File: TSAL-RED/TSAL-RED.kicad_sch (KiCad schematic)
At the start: 49 parts, among them J1 Conn_01x02, J2 Conn_01x02, J3 Conn_02x01, J4 Conn_02x01, K1 G5V-2, Q1 2N7002, Q2 AO3401A, U1 LM358, U2 4N35, U3 NE555D

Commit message: CREATE TSAL PCBs
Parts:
- added J5: Conn_02x01, Connector_Molex:Molex_Micro-Fit_3.0_43045-0212_2x01_P3.00mm_Vertical, symbol Connector_Generic:Conn_02x01
- J1, J2: footprint Connector_Molex:Molex_Micro-Fit_3.0_43650-0215_1x02_P3.00mm_Vertical -> Connector_Molex:Molex_Mini-Fit_Jr_5566-02A_2x01_P4.20mm_Vertical
- R10, R11, R29, R7, R8, R9: footprint Resistor_SMD:R_0201_0603Metric_Pad0.64x0.40mm_HandSolder -> Resistor_SMD:R_0603_1608Metric_Pad0.98x0.95mm_HandSolder
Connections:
- net GLV+: now also J5.1 (Pin_1)
- net GLV-: now also J5.2 (Pin_2)
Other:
- note added: "POWER"
- company: (none) -> Formula Barton Racing
- title: (none) -> TSAL RED and DIscharge
- moved on the sheet: D4, J3, J4, R29

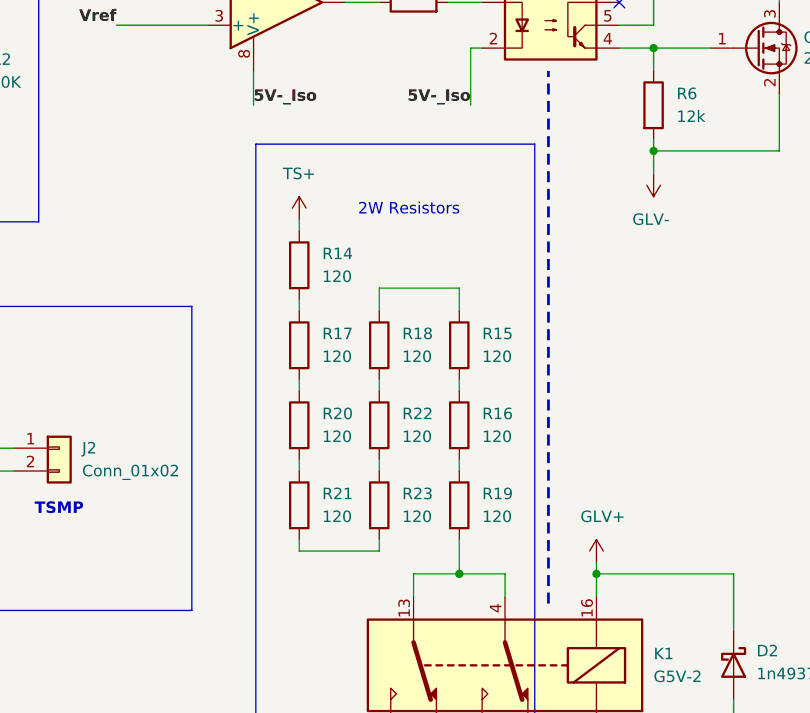
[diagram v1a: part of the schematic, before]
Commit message: Modify TSAL PCB and use relative paths for libraries
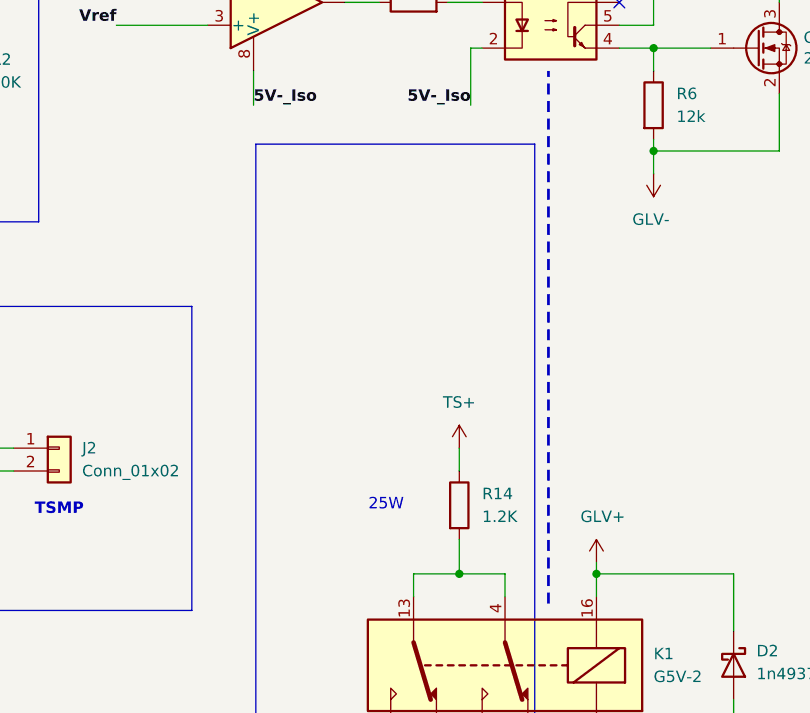
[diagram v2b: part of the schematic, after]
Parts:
- removed R15, R16, R17, R18, R19, R20, R21, R22, R23: 120, Resistor_THT:R_Axial_DIN0516_L15.5mm_D5.0mm_P20.32mm_Horizontal, symbol Device:R
- R14: value 120 -> 1.2K; footprint Resistor_THT:R_Axial_DIN0516_L15.5mm_D5.0mm_P20.32mm_Horizontal -> Chassis_Resistor:HSA25
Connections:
- net at R14.2: now also K1.13, K1.4
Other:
- note added: "25W"
- note removed: "2W Resistors"

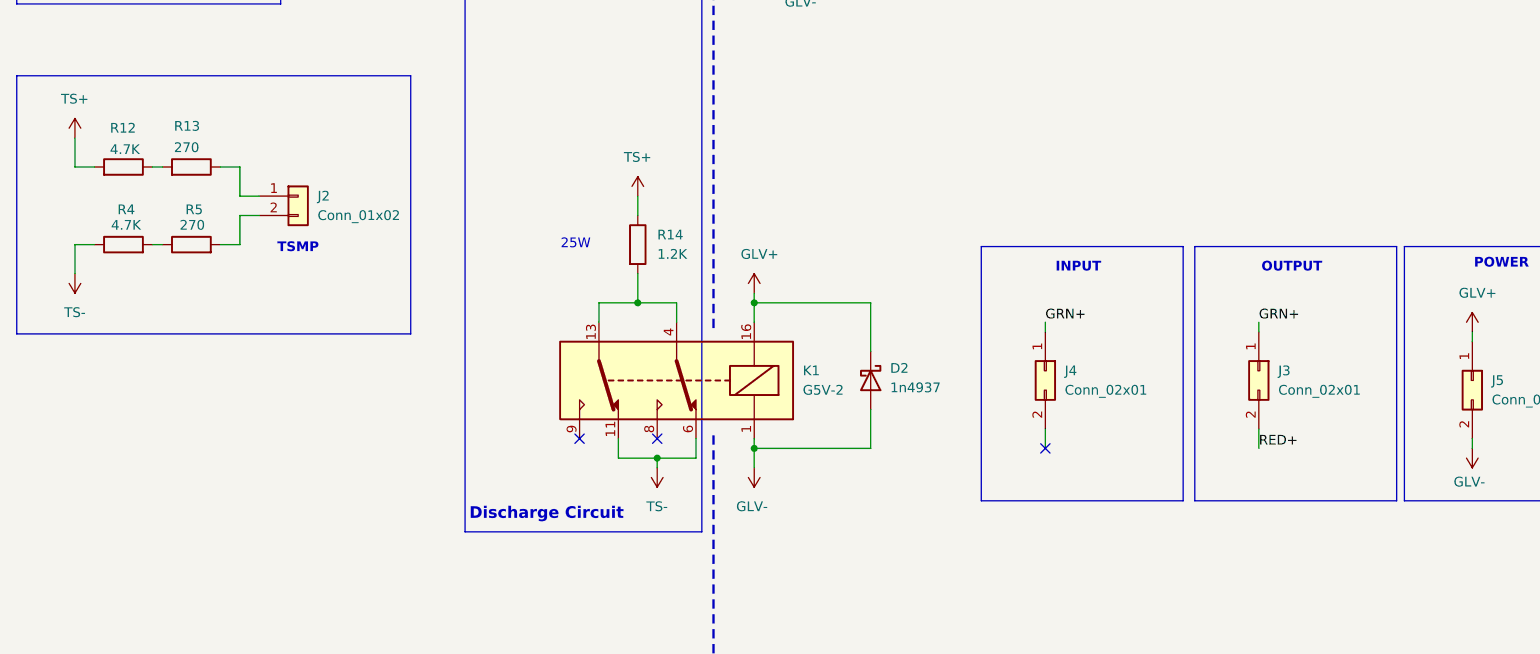
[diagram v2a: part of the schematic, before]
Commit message: Single signal connector
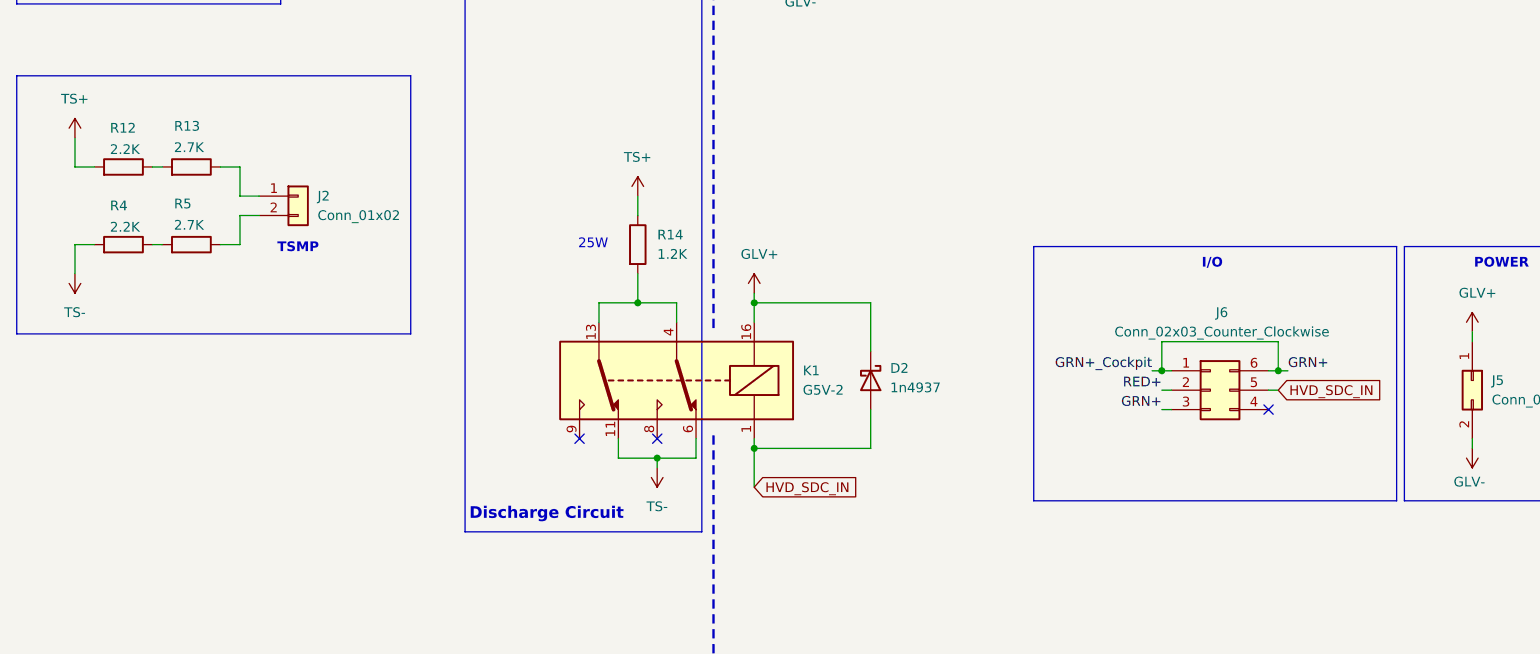
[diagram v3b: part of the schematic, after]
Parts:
- removed J3, J4: Conn_02x01, Connector_Molex:Molex_Micro-Fit_3.0_43045-0212_2x01_P3.00mm_Vertical, symbol Connector_Generic:Conn_02x01
- added J6: Conn_02x03_Counter_Clockwise, Connector_Molex:Molex_Micro-Fit_3.0_43045-0612_2x03_P3.00mm_Vertical, symbol Connector_Generic:Conn_02x03_Counter_Clockwise
- R12, R4: value 4.7K -> 2.2K; footprint Resistor_SMD:R_0805_2012Metric_Pad1.20x1.40mm_HandSolder -> Resistor_THT:R_Axial_DIN0414_L11.9mm_D4.5mm_P15.24mm_Horizontal
- R13, R5: value 270 -> 2.7K; footprint Resistor_SMD:R_0805_2012Metric_Pad1.20x1.40mm_HandSolder -> Resistor_THT:R_Axial_DIN0414_L11.9mm_D4.5mm_P15.24mm_Horizontal
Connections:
- net GLV-: no longer D2.2 (A), K1.1
- net GRN+: now also J6.1 (Pin_1), J6.3 (Pin_3), J6.6 (Pin_6)
- net RED+: now also J6.2 (Pin_2)
- net TS-: now also R4.2; no longer R4.1
- net at R5.1: now also J2.2 (Pin_2); no longer R4.2
- net at R5.2: now also R4.1; no longer J2.2 (Pin_2)
- new net HVD_SDC_IN: D2.2 (A), J6.5 (Pin_5), K1.1
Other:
- note added: "I/O"
- note removed: "INPUT"
- note removed: "OUTPUT"

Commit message: update check
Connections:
- net GLV-: now also J6.4 (Pin_4)
- no-connect marks 4 -> 3
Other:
- title: TSAL RED and DIscharge -> TSAL RED and Discharge
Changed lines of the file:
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@@
 	(paper "A3")
 	(title_block
-		(title "TSAL RED and DIscharge")
+		(title "TSAL RED and Discharge")
 		(date "2025-01-03")
-		(rev "1.2")
+		(rev "1.2.1")
 		(company "Formula Barton Racing")
 		(comment 1 "evanscesil@gmail.com")
@@
 		(at 170.18 166.37)
 	)
-	(no_connect
-		(at 260.35 162.56)
-	)
 	(wire
 		(pts
@@
 	(wire
 		(pts
+			(xy 261.62 162.56) (xy 260.35 162.56)
+		)
+		(stroke
+			(width 0)
+			(type default)
+		)
+	)
+	(wire
+		(pts
 			(xy 284.48 83.82) (xy 279.4 83.82)
 		)
@@
 	(label "RED+"
 		(at 311.15 82.55 180)
-		(fields_autoplaced yes)
 		(effects
 			(font
@@
 	(label "5V-_Iso"
 		(at 144.78 233.68 180)
-		(fields_autoplaced yes)
 		(effects
 			(font
@@
 	(label "GRN+_Cockpit"
 		(at 245.11 157.48 180)
-		(fields_autoplaced yes)
 		(effects
 			(font
@@
 	(label "5V+_Iso"
 		(at 144.78 204.47 180)
-		(fields_autoplaced yes)
 		(effects
 			(font
@@
 	(label "Vref"
 		(at 140.97 222.25 180)
-		(fields_autoplaced yes)
 		(effects
 			(font
@@
 	(label "5V-_Iso"
 		(at 170.18 231.14 180)
-		(fields_autoplaced yes)
 		(effects
 			(font
@@
 	(label "5V+_Iso"
 		(at 154.94 69.85 0)
-		(fields_autoplaced yes)
 		(effects
 			(font
@@
 	(label "5V-_Iso"
 		(at 154.94 96.52 0)
-		(fields_autoplaced yes)
 		(effects
 			(font
@@
 	(label "5V-_Iso"
 		(at 179.07 96.52 180)
-		(fields_autoplaced yes)
 		(effects
 			(font
@@
 	(label "TS+"
 		(at 107.95 86.36 0)
-		(fields_autoplaced yes)
 		(effects
 			(font
@@
 	(label "Vin"
 		(at 139.7 82.55 180)
-		(fields_autoplaced yes)
 		(effects
 			(font
@@
 	(label "GRN+"
 		(at 321.31 140.97 0)
-		(fields_autoplaced yes)
 		(effects
 			(font
@@
 	(label "GRN+"
 		(at 246.38 162.56 180)
-		(fields_autoplaced yes)
 		(effects
 			(font
@@
 	(label "RED+"
 		(at 246.38 160.02 180)
-		(fields_autoplaced yes)
 		(effects
 			(font
@@
 	(label "Vref"
 		(at 139.7 87.63 180)
-		(fields_autoplaced yes)
 		(effects
 			(font
@@
 	(label "TS-"
 		(at 107.95 99.06 0)
-		(fields_autoplaced yes)
 		(effects
 			(font
@@
 	(label "5V+_Iso"
 		(at 170.18 209.55 180)
-		(fields_autoplaced yes)
 		(effects
 			(font
@@
 	(label "GRN+"
 		(at 262.89 157.48 0)
-		(fields_autoplaced yes)
 		(effects
 			(font
@@
 					(unit 1)
 				)
+			)
+		)
+	)
+	(symbol
+		(lib_id "power-symbol-library:GLV-")
+		(at 261.62 162.56 180)
+		(unit 1)
+		(exclude_from_sim no)
+		(in_bom yes)
+		(on_board yes)
+		(dnp no)
+		(property "Reference" "#PWR012"
+			(at 261.62 158.75 0)
+			(effects
+				(font
+					(size 1.27 1.27)
+				)
+				(hide yes)
+			)
+		)
+		(property "Value" "GLV-"
+			(at 261.239 166.9542 0)
+			(effects
+				(font
+					(size 1.27 1.27)
+				)
+			)
+		)
+		(property "Footprint" ""
+			(at 261.62 162.56 0)
+			(effects
+				(font
+					(size 1.27 1.27)
+				)
+				(hide yes)
+			)
+		)
+		(property "Datasheet" ""
+			(at 261.62 162.56 0)
+			(effects
+				(font
+					(size 1.27 1.27)
+				)
+				(hide yes)
+			)
+		)
+		(property "Description" ""
+			(at 261.62 162.56 0)
+			(effects
+				(font
+					(size 1.27 1.27)
+				)
+				(hide yes)
+			)
+		)
+		(pin "1"
+		)
+		(instances
+			(project "TSAL-RED"
+				(path "/3dba08e1-8d4d-49dd-80dc-41df92bd5b0c"
+					(reference "#PWR012")
+					(unit 1)
+				)

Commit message: Precharge modifications
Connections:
- net GLV+: no longer D2.1 (K), K1.16
- net GLV-: now also J6.3 (Pin_3); no longer J6.4 (Pin_4)
- net GRN+: no longer J6.3 (Pin_3)
- net HVD_SDC_IN renamed TSAC_GLV-
- net TSAC_GLV-: now also J6.4 (Pin_4); no longer J6.5 (Pin_5)
- new net AIR+_Sup: D2.1 (K), J6.5 (Pin_5), K1.16
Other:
- note added: "Note: TSAC_GLV is GLV but taken from inside the accumulator AIR+_Sup is the SDC supply"
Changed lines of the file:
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@@
 		(title "TSAL RED and Discharge")
 		(date "2025-01-03")
-		(rev "1.2.1")
+		(rev "1.3")
 		(company "Formula Barton Racing")
 		(comment 1 "evanscesil@gmail.com")
@@
 		)
 	)
+	(text "Note: TSAC_GLV is GLV but taken from inside the accumulator\n	 AIR+_Sup is the SDC supply"
+		(exclude_from_sim no)
+		(at 229.362 178.562 0)
+		(effects
+			(font
+				(size 1.524 1.524)
+				(thickness 0.254)
+				(bold yes)
+			)
+			(justify left)
+		)
+	)
 	(text "POWER"
 		(exclude_from_sim no)
@@
 	(wire
 		(pts
-			(xy 193.04 147.32) (xy 193.04 148.59)
+			(xy 193.04 144.78) (xy 193.04 148.59)
 		)
 		(stroke
@@
 	(wire
 		(pts
+			(xy 246.38 162.56) (xy 247.65 162.56)
+		)
+		(stroke
+			(width 0)
+			(type default)
+		)
+	)
+	(wire
+		(pts
 			(xy 140.97 222.25) (xy 144.78 222.25)
 		)
@@
 	(wire
 		(pts
+			(xy 246.38 163.83) (xy 246.38 162.56)
+		)
+		(stroke
+			(width 0)
+			(type default)
+		)
+	)
+	(wire
+		(pts
 			(xy 284.48 87.63) (xy 284.48 83.82)
 		)
@@
 	(wire
 		(pts
-			(xy 246.38 162.56) (xy 247.65 162.56)
-		)
-		(stroke
-			(width 0)
-			(type default)
-		)
-	)
-	(wire
-		(pts
 			(xy 201.93 224.79) (xy 201.93 227.33)
 		)
@@
 		)
 	)
-	(label "GRN+"
-		(at 246.38 162.56 180)
-		(effects
-			(font
-				(size 1.27 1.27)
-			)
-			(justify right bottom)
-		)
-	)
 	(label "RED+"
 		(at 246.38 160.02 180)
@@
 		)
 	)
-	(global_label "HVD_SDC_IN"
+	(global_label "TSAC_GLV-"
 		(shape input)
 		(at 193.04 172.72 0)
@@
 		)
 		(property "Intersheetrefs" "${INTERSHEET_REFS}"
-			(at 207.3343 172.72 0)
+			(at 206.4876 172.72 0)
 			(effects
 				(font
@@
 		)
 	)
-	(global_label "HVD_SDC_IN"
+	(global_label "AIR+_Sup"
 		(shape input)
 		(at 261.62 160.02 0)
@@
 		)
 		(property "Intersheetrefs" "${INTERSHEET_REFS}"
-			(at 275.9143 160.02 0)
+			(at 273.6161 160.02 0)
+			(effects
+				(font
+					(size 1.27 1.27)
+				)
+				(justify left)
+				(hide yes)
+			)
+		)
+	)
+	(global_label "AIR+_Sup"
+		(shape input)
+		(at 193.04 144.78 0)
+		(fields_autoplaced yes)
+		(effects
+			(font
+				(size 1.27 1.27)
+			)
+			(justify left)
+		)
+		(property "Intersheetrefs" "${INTERSHEET_REFS}"
+			(at 205.0361 144.78 0)
+			(effects
+				(font
+					(size 1.27 1.27)
+				)
+				(justify left)
+				(hide yes)
+			)
+		)
+	)
+	(global_label "TSAC_GLV-"
+		(shape input)
+		(at 261.62 162.56 0)
+		(fields_autoplaced yes)
+		(effects
+			(font
+				(size 1.27 1.27)
+			)
+			(justify left)
+		)
+		(property "Intersheetrefs" "${INTERSHEET_REFS}"
+			(at 275.0676 162.56 0)
 			(effects
 				(font
@@
 	)
 	(symbol
-		(lib_id "power:+12V")
-		(at 193.04 147.32 0)
-		(unit 1)
-		(exclude_from_sim no)
-		(in_bom yes)
-		(on_board yes)
-		(dnp no)
-		(property "Reference" "#PWR011"
-			(at 193.04 151.13 0)
-			(effects
-				(font
-					(size 1.27 1.27)
-				)
-				(hide yes)
-			)
-		)
-		(property "Value" "GLV+"
-			(at 191.262 142.24 0)
-			(effects
-				(font
-					(size 1.27 1.27)
-				)
-				(justify left)
-			)
-		)
-		(property "Footprint" ""
-			(at 193.04 147.32 0)
-			(effects
-				(font
-					(size 1.27 1.27)
-				)
-				(hide yes)
-			)
-		)
-		(property "Datasheet" ""
-			(at 193.04 147.32 0)
-			(effects
-				(font
-					(size 1.27 1.27)
-				)
-				(hide yes)
-			)
-		)
-		(property "Description" ""
-			(at 193.04 147.32 0)
-			(effects
-				(font
-					(size 1.27 1.27)
-				)
-				(hide yes)
-			)
-		)
-		(pin "1"
-		)
-		(instances
-			(project "TSAL-RED"
-				(path "/3dba08e1-8d4d-49dd-80dc-41df92bd5b0c"
-					(reference "#PWR011")
-					(unit 1)
-				)
-			)
-		)
-	)
-	(symbol
 		(lib_id "Timer:NE555D")
 		(at 262.89 78.74 0)
@@
 	)
 	(symbol
+		(lib_id "power-symbol-library:GLV-")
+		(at 246.38 163.83 180)
+		(unit 1)
+		(exclude_from_sim no)
+		(in_bom yes)
+		(on_board yes)
+		(dnp no)
+		(property "Reference" "#PWR019"
+			(at 246.38 160.02 0)
+			(effects
+				(font
+					(size 1.27 1.27)
+				)
+				(hide yes)
+			)
+		)
+		(property "Value" "GLV-"
+			(at 245.999 168.2242 0)
+			(effects
+				(font
+					(size 1.27 1.27)
+				)
+			)
+		)
+		(property "Footprint" ""
+			(at 246.38 163.83 0)
+			(effects
+				(font
+					(size 1.27 1.27)
+				)
+				(hide yes)
+			)
+		)
+		(property "Datasheet" ""
+			(at 246.38 163.83 0)
+			(effects
+				(font
+					(size 1.27 1.27)
+				)
+				(hide yes)
+			)
+		)
+		(property "Description" ""
+			(at 246.38 163.83 0)
+			(effects
+				(font
+					(size 1.27 1.27)
+				)
+				(hide yes)
+			)
+		)
+		(pin "1"
+		)
+		(instances
+			(project "TSAL-RED"
+				(path "/3dba08e1-8d4d-49dd-80dc-41df92bd5b0c"
+					(reference "#PWR019")
+					(unit 1)
+				)
+			)
+		)
+	)
+	(symbol
 		(lib_id "Device:R")
 		(at 119.38 130.81 270)
@@
 					(unit 1)
 				)
-			)
-		)
-	)
-	(symbol
-		(lib_id "power-symbol-library:GLV-")
-		(at 261.62 162.56 180)
-		(unit 1)
-		(exclude_from_sim no)
-		(in_bom yes)
-		(on_board yes)
-		(dnp no)
-		(property "Reference" "#PWR012"
-			(at 261.62 158.75 0)
-			(effects
-				(font
-					(size 1.27 1.27)
-				)
-				(hide yes)
-			)
-		)
-		(property "Value" "GLV-"
-			(at 261.239 166.9542 0)
-			(effects
-				(font
-					(size 1.27 1.27)
-				)
-			)
-		)
-		(property "Footprint" ""
-			(at 261.62 162.56 0)
-			(effects
-				(font
-					(size 1.27 1.27)
-				)
-				(hide yes)
-			)
-		)
-		(property "Datasheet" ""
-			(at 261.62 162.56 0)
-			(effects
-				(font
-					(size 1.27 1.27)
-				)
-				(hide yes)
-			)
-		)
-		(property "Description" ""
-			(at 261.62 162.56 0)
-			(effects
-				(font
-					(size 1.27 1.27)
-				)
-				(hide yes)
-			)
-		)
-		(pin "1"
-		)
-		(instances
-			(project "TSAL-RED"
-				(path "/3dba08e1-8d4d-49dd-80dc-41df92bd5b0c"
-					(reference "#PWR012")
-					(unit 1)
-				)

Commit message: Add latest circuit PDFs
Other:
- note added: "Note: TSAC_GLV is GLV but taken from inside the accumulator AIR+_Sup is the SDC supply (Also +ve input of AIR+)"
- note removed: "Note: TSAC_GLV is GLV but taken from inside the accumulator AIR+_Sup is the SDC supply"
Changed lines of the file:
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@@
 		)
 	)
-	(text "Note: TSAC_GLV is GLV but taken from inside the accumulator\n	 AIR+_Sup is the SDC supply"
+	(text "Note: TSAC_GLV is GLV but taken from inside the accumulator\n	 AIR+_Sup is the SDC supply (Also +ve input of AIR+)"
 		(exclude_from_sim no)
 		(at 229.362 178.562 0)
@@
 	(wire
 		(pts
-			(xy 193.04 144.78) (xy 193.04 148.59)
+			(xy 193.04 143.51) (xy 193.04 148.59)
 		)
 		(stroke
@@
 			(font
 				(size 1.27 1.27)
+				(thickness 0.254)
+				(bold yes)
 			)
 			(justify left)
 		)
 		(property "Intersheetrefs" "${INTERSHEET_REFS}"
-			(at 206.4876 172.72 0)
+			(at 206.9636 172.72 0)
 			(effects
 				(font
@@
 	(global_label "AIR+_Sup"
 		(shape input)
-		(at 193.04 144.78 0)
+		(at 193.04 143.51 0)
 		(fields_autoplaced yes)
 		(effects
 			(font
 				(size 1.27 1.27)
+				(thickness 0.254)
+				(bold yes)
 			)
 			(justify left)
 		)
 		(property "Intersheetrefs" "${INTERSHEET_REFS}"
-			(at 205.0361 144.78 0)
+			(at 205.5121 143.51 0)
 			(effects
 				(font

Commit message: Add PDIST
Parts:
- added R15: 270, Resistor_SMD:R_1206_3216Metric_Pad1.30x1.75mm_HandSolder, symbol Device:R
- R28: value 910 -> 180
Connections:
- net TS-: now also R15.2; no longer R2.2
- net Vin renamed V_Cap
- new net: R15.1, R2.2
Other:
- note added: "1.77V"
- note added: "1.77V at 58.8V"
- note removed: "1.73V"
- note removed: "1.73V at 58.8V"
- moved on the sheet: R2
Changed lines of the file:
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@@
 	(title_block
 		(title "TSAL RED and Discharge")
-		(date "2025-01-03")
-		(rev "1.3")
+		(date "2025-04-26")
+		(rev "1.4")
 		(company "Formula Barton Racing")
 		(comment 1 "evanscesil@gmail.com")
@@
 		)
 	)
-	(text "1.73V at 58.8V\n"
+	(text "1.77V at 58.8V\n"
 		(exclude_from_sim no)
 		(at 140.208 78.74 0)
@@
 		)
 	)
-	(text "1.73V\n"
+	(text "1.77V\n"
 		(exclude_from_sim no)
 		(at 138.176 225.044 0)
@@
 	(wire
 		(pts
+			(xy 123.19 93.98) (xy 123.19 92.71)
+		)
+		(stroke
+			(width 0)
+			(type default)
+		)
+	)
+	(wire
+		(pts
 			(xy 262.89 88.9) (xy 262.89 100.33)
 		)
@@
 	(wire
 		(pts
-			(xy 123.19 82.55) (xy 123.19 88.9)
+			(xy 123.19 82.55) (xy 123.19 85.09)
 		)
 		(stroke
@@
 	(wire
 		(pts
-			(xy 123.19 96.52) (xy 123.19 101.6)
-		)
-		(stroke
-			(width 0)
-			(type default)
-		)
-	)
-	(wire
-		(pts
 			(xy 107.95 81.28) (xy 107.95 82.55)
 		)
@@
 		)
 	)
-	(label "Vin"
+	(label "V_Cap"
 		(at 139.7 82.55 180)
 		(effects
@@
 	(symbol
 		(lib_id "Device:R")
-		(at 123.19 92.71 0)
+		(at 123.19 88.9 0)
 		(unit 1)
 		(exclude_from_sim no)
@@
 		(fields_autoplaced yes)
 		(property "Reference" "R2"
-			(at 125.73 91.4399 0)
+			(at 125.73 87.6299 0)
 			(effects
 				(font
@@
 		)
 		(property "Value" "10K"
-			(at 125.73 93.9799 0)
+			(at 125.73 90.1699 0)
 			(effects
 				(font
@@
 		)
 		(property "Footprint" "Resistor_SMD:R_1206_3216Metric_Pad1.30x1.75mm_HandSolder"
-			(at 121.412 92.71 90)
+			(at 121.412 88.9 90)
 			(effects
 				(font
@@
 		)
 		(property "Datasheet" "~"
-			(at 123.19 92.71 0)
+			(at 123.19 88.9 0)
 			(effects
 				(font
@@
 		)
 		(property "Description" "Resistor"
-			(at 123.19 92.71 0)
+			(at 123.19 88.9 0)
 			(effects
 				(font
@@
 			)
 		)
-		(property "Value" "910"
+		(property "Value" "180"
 			(at 147.32 210.8199 0)
 			(effects
@@
 					(unit 1)
 				)
+			)
+		)
+	)
+	(symbol
+		(lib_id "Device:R")
+		(at 123.19 97.79 0)
+		(unit 1)
+		(exclude_from_sim no)
+		(in_bom yes)
+		(on_board yes)
+		(dnp no)
+		(fields_autoplaced yes)
+		(property "Reference" "R15"
+			(at 125.73 96.5199 0)
+			(effects
+				(font
+					(size 1.27 1.27)
+				)
+				(justify left)
+			)
+		)
+		(property "Value" "270"
+			(at 125.73 99.0599 0)
+			(effects
+				(font
+					(size 1.27 1.27)
+				)
+				(justify left)
+			)
+		)
+		(property "Footprint" "Resistor_SMD:R_1206_3216Metric_Pad1.30x1.75mm_HandSolder"
+			(at 121.412 97.79 90)
+			(effects
+				(font
+					(size 1.27 1.27)
+				)
+				(hide yes)
+			)
+		)
+		(property "Datasheet" "~"
+			(at 123.19 97.79 0)
+			(effects
+				(font
+					(size 1.27 1.27)
+				)
+				(hide yes)
+			)
+		)
+		(property "Description" "Resistor"
+			(at 123.19 97.79 0)
+			(effects
+				(font
+					(size 1.27 1.27)
+				)
+				(hide yes)
+			)
+		)
+		(pin "2"
+		)
+		(pin "1"
+		)
+		(instances
+			(project "TSAL-RED"
+				(path "/3dba08e1-8d4d-49dd-80dc-41df92bd5b0c"
+					(reference "R15")
+					(unit 1)
+				)
